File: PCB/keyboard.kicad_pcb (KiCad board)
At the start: 2 copper layers, 74 parts, among them J1 USB4510-03-1-A, J4 switch, U1 NCP1117LPST33T3G, U2 USBLC6-2SC6, U3 USBLC6-2SC6, U4 RP2040, U5 W25Q128JVS, Y1 12MHz

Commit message: Update footprint library
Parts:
- added D101: DIODE, Diode_SMD:D_SOD-123, F.Cu at (274.3, 106.7)
- added D102: DIODE, Diode_SMD:D_SOD-123, F.Cu at (262.8, 106.7)
- added D104: DIODE, Diode_SMD:D_SOD-123, F.Cu at (268.6, 110.0)
- added D105: DIODE, Diode_SMD:D_SOD-123, F.Cu at (280.1, 110.0)
- added D106: DIODE, Diode_SMD:D_SOD-123, F.Cu at (274.3, 110.0)
- added D107: DIODE, Diode_SMD:D_SOD-123, F.Cu at (280.1, 106.7)
- added D108: DIODE, Diode_SMD:D_SOD-123, F.Cu at (285.8, 106.7)
- added D109: DIODE, Diode_SMD:D_SOD-123, F.Cu at (262.8, 110.0)
- added D110: DIODE, Diode_SMD:D_SOD-123, F.Cu at (274.3, 116.7)
- added D111: DIODE, Diode_SMD:D_SOD-123, F.Cu at (268.6, 120.1)
- added D112: DIODE, Diode_SMD:D_SOD-123, F.Cu at (268.6, 113.4)
- added D113: DIODE, Diode_SMD:D_SOD-123, F.Cu at (268.6, 116.7)
- added D114: DIODE, Diode_SMD:D_SOD-123, F.Cu at (262.8, 116.7)
- added D115: DIODE, Diode_SMD:D_SOD-123, F.Cu at (268.6, 106.7)
- added D116: DIODE, Diode_SMD:D_SOD-123, F.Cu at (262.8, 113.4)
- added D117: DIODE, Diode_SMD:D_SOD-123, F.Cu at (262.8, 123.4)
- added D118: DIODE, Diode_SMD:D_SOD-123, F.Cu at (262.8, 120.1)
- added DD103: DIODE, Diode_SMD:D_SOD-123, F.Cu at (274.3, 113.4)
- added MX101: SW_Push, Footprints:CherryMX_Choc_Hotswap, F.Cu at (341.0, 47.1)
- added MX102: SW_Push, Footprints:CherryMX_Choc_Hotswap, F.Cu at (271.5, 93.4)
- added MX103: SW_Push, Footprints:CherryMX_Choc_Hotswap, F.Cu at (271.5, 70.3)
- added MX104: SW_Push, Footprints:CherryMX_Choc_Hotswap, F.Cu at (271.5, 47.1)
- added MX105: SW_Push, Footprints:CherryMX_Choc_Hotswap, F.Cu at (294.7, 93.4)
- added MX106: SW_Push, Footprints:CherryMX_Choc_Hotswap, F.Cu at (317.8, 47.1)
- added MX107: SW_Push, Footprints:CherryMX_Choc_Hotswap, F.Cu at (317.8, 70.3)
- added MX108: SW_Push, Footprints:CherryMX_Choc_Hotswap, F.Cu at (364.1, 93.4)
- added MX109: SW_Push, Footprints:CherryMX_Choc_Hotswap, F.Cu at (364.1, 47.1)
- added MX110: SW_Push, Footprints:CherryMX_Choc_Hotswap, F.Cu at (294.7, 47.1)
- added MX111: SW_Push, Footprints:CherryMX_Choc_Hotswap, F.Cu at (341.0, 70.3)
- added MX112: SW_Push, Footprints:CherryMX_Choc_Hotswap, F.Cu at (387.3, 70.3)
- added MX113: SW_Push, Footprints:CherryMX_Choc_Hotswap, F.Cu at (387.3, 93.4)
- added MX114: SW_Push, Footprints:CherryMX_Choc_Hotswap, F.Cu at (387.3, 47.1)
- added MX115: SW_Push, Footprints:CherryMX_Choc_Hotswap, F.Cu at (364.1, 70.3)
- added MX116: SW_Push, Footprints:CherryMX_Choc_Hotswap, F.Cu at (294.7, 70.3)
- added MX117: SW_Push, Footprints:CherryMX_Choc_Hotswap, F.Cu at (341.0, 93.4)
- added MX118: SW_Push, Footprints:CherryMX_Choc_Hotswap, F.Cu at (317.8, 93.4)
- added U1: TPS54202DDC, Package_TO_SOT_SMD:SOT-23-6, F.Cu at (291.3, 107.2)
- MX201: renamed from MX1; footprint Keyboard:MX -> Footprints:CherryMX_Choc_Hotswap
- MX202: renamed from MX2; footprint Keyboard:MX -> Footprints:CherryMX_Choc_Hotswap
- MX203: renamed from MX3; footprint Keyboard:MX -> Footprints:CherryMX_Choc_Hotswap
- MX204: renamed from MX4; footprint Keyboard:MX -> Footprints:CherryMX_Choc_Hotswap
- MX205: renamed from MX5; footprint Keyboard:MX -> Footprints:CherryMX_Choc_Hotswap
- MX206: renamed from MX6; footprint Keyboard:MX -> Footprints:CherryMX_Choc_Hotswap
- MX207: renamed from MX7; footprint Keyboard:MX -> Footprints:CherryMX_Choc_Hotswap
- MX208: renamed from MX8; footprint Keyboard:MX -> Footprints:CherryMX_Choc_Hotswap
- MX209: renamed from MX9; footprint Keyboard:MX -> Footprints:CherryMX_Choc_Hotswap
- MX210: renamed from MX10; footprint Keyboard:MX -> Footprints:CherryMX_Choc_Hotswap
- MX211: renamed from MX11; footprint Keyboard:MX -> Footprints:CherryMX_Choc_Hotswap
- MX212: renamed from MX12; footprint Keyboard:MX -> Footprints:CherryMX_Choc_Hotswap
- MX213: renamed from MX13; footprint Keyboard:MX -> Footprints:CherryMX_Choc_Hotswap
- MX214: renamed from MX14; footprint Keyboard:MX -> Footprints:CherryMX_Choc_Hotswap
- MX215: renamed from MX15; footprint Keyboard:MX -> Footprints:CherryMX_Choc_Hotswap
- MX216: renamed from MX16; footprint Keyboard:MX -> Footprints:CherryMX_Choc_Hotswap
- MX217: renamed from MX17; footprint Keyboard:MX -> Footprints:CherryMX_Choc_Hotswap
- MX218: renamed from MX18; footprint Keyboard:MX -> Footprints:CherryMX_Choc_Hotswap
- U5: value W25Q128JVS -> W25Q128JVSIQ
- renumbered D3 to D201, D2 to D202, D1 to D203, D6 to D204, D5 to D205, D4 to D206, D9 to D207, D8 to D208, D7 to D209, D12 to D210, D11 to D211, D10 to D212, D15 to D213, D14 to D214, D13 to D215, D18 to D216, D17 to D217, D16 to D218, J1 to J101, R8 to R108, R9 to R109
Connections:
- C16 pad 1: Net-(C16-Pad1) -> /XIN
- D201 pad 1: ROW1 -> L-ROW-1
- D202 pad 1: ROW2 -> L-ROW-2
- D203 pad 1: ROW3 -> L-ROW-3
- D204 pad 1: ROW1 -> L-ROW-1
- D205 pad 1: ROW2 -> L-ROW-2
- D206 pad 1: ROW3 -> L-ROW-3
- D207 pad 1: ROW1 -> L-ROW-1
- D208 pad 1: ROW2 -> L-ROW-2
- D209 pad 1: ROW3 -> L-ROW-3
- D210 pad 1: ROW1 -> L-ROW-1
- D211 pad 1: ROW2 -> L-ROW-2
- D212 pad 1: ROW3 -> L-ROW-3
- D213 pad 1: ROW1 -> L-ROW-1
- D214 pad 1: ROW2 -> L-ROW-2
- D215 pad 1: ROW3 -> L-ROW-3
- D216 pad 1: ROW1 -> L-ROW-1
- D217 pad 1: ROW2 -> L-ROW-2
- D218 pad 1: ROW3 -> L-ROW-3
- MX201 pad 1: COL1 -> L-COL-1
- MX202 pad 1: COL1 -> L-COL-1
- MX203 pad 1: COL1 -> L-COL-1
- MX204 pad 1: COL2 -> L-COL-2
- MX205 pad 1: COL2 -> L-COL-2
- MX206 pad 1: COL2 -> L-COL-2
- MX207 pad 1: COL3 -> L-COL-3
- MX208 pad 1: COL3 -> L-COL-3
- MX209 pad 1: COL3 -> L-COL-3
- MX210 pad 1: COL4 -> L-COL-4
- MX211 pad 1: COL4 -> L-COL-4
- MX212 pad 1: COL4 -> L-COL-4
- MX213 pad 1: COL5 -> L-COL-5
- MX214 pad 1: COL5 -> L-COL-5
- MX215 pad 1: COL5 -> L-COL-5
- MX216 pad 1: COL6 -> L-COL-6
- MX217 pad 1: COL6 -> L-COL-6
- MX218 pad 1: COL6 -> L-COL-6
- Y1 pad 1: Net-(C16-Pad1) -> /XIN
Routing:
- net ROW2: track 95.0 -> 0.00 mm, vias 5 -> 0
- net L-ROW-2: track 0.00 -> 95.0 mm, vias 0 -> 5
- net L-ROW-3: track 0.00 -> 94.6 mm, vias 0 -> 3
- net ROW1: track 91.8 -> 0.00 mm, vias 5 -> 0
- net L-ROW-1: track 0.00 -> 91.8 mm, vias 0 -> 5
- net ROW3: track 90.2 -> 0.00 mm, vias 3 -> 0
- net L-COL-5: track 0.00 -> 47.1 mm
- net L-COL-3: track 0.00 -> 42.6 mm
- net L-COL-2: track 0.00 -> 38.1 mm
- net COL2: track 38.1 -> 0.00 mm
- net L-COL-1: track 0.00 -> 38.1 mm
- net COL1: track 38.1 -> 0.00 mm
- net L-COL-4: track 0.00 -> 38.1 mm
- net COL5: track 38.1 -> 0.00 mm
- net COL4: track 38.1 -> 0.00 mm
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
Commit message: wip full sch
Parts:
- D101, D102, D104, D105, D106, D107, D108, D109, D110, D111, D112, D113, D114, D115, D116, D117, D118, DD103: moved to B.Cu
- moved C13 124.1 mm to (168.6, 61.0), turned to 90 degrees
- moved C14 120.4 mm to (166.3, 61.0), turned to 90 degrees
- moved U1 106.2 mm to (193.2, 66.5), turned to 90 degrees
- moved D113 106.0 mm to (353.9, 53.8), turned to 90 degrees
- moved J4 102.6 mm to (193.2, 53.0)
- moved D114 101.1 mm to (353.9, 72.8), turned to 90 degrees
- moved C11 88.0 mm to (155.5, 124.3)
- moved C12 88.0 mm to (152.6, 124.3)
- moved C16 88.0 mm to (149.8, 124.3)
- moved C7 88.0 mm to (158.4, 124.3)
- moved R109 88.0 mm to (169.9, 124.3)
- moved R13 88.0 mm to (178.6, 124.3)
- moved R5 88.0 mm to (172.8, 124.3)
- moved R7 88.0 mm to (181.5, 124.3)
- moved C6 88.0 mm to (161.3, 124.3)
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
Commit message: latest changes
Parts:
- removed C1, C2: 10u, Capacitor_SMD:C_0603_1608Metric
- removed C10, C11, C12, C15, C4, C5, C6, C7, C8, C9: 100n, Capacitor_SMD:C_0402_1005Metric
- removed C13, C14: 1u, Capacitor_SMD:C_0402_1005Metric
- removed C16, C17: 20p, Capacitor_SMD:C_0402_1005Metric
- removed C3: 10u, Capacitor_SMD:C_0805_2012Metric
- removed D19: C2480, Diode_SMD:D_SMA
- removed DD103: DIODE, Diode_SMD:D_SOD-123
- removed F2: 1000mA, Fuse:Fuse_1206_3216Metric
- removed J4: switch, Connector_PinHeader_2.54mm:PinHeader_1x02_P2.54mm_Vertical
- removed R1, R2: 5.1k, Resistor_SMD:R_0603_1608Metric
- removed R12, R13: 2.2K, Resistor_SMD:R_0402_1005Metric
- removed R3, R4: 27, Resistor_SMD:R_0402_1005Metric
- removed R5: 10k, Resistor_SMD:R_0402_1005Metric
- removed R6, R7: 1k, Resistor_SMD:R_0402_1005Metric
- removed U1: TPS54202DDC, Package_TO_SOT_SMD:SOT-23-6
- removed U1: NCP1117LPST33T3G, NCP1117LPST33T3G:NCP1117LPST33T3G
- removed U2, U3: USBLC6-2SC6, Package_TO_SOT_SMD:SOT-23-6
- removed U4: RP2040, RP2040:SC090813
- removed U5: W25Q128JVSIQ, Package_SO:SOIC-8_5.23x5.23mm_P1.27mm
- removed Y1: 12MHz, Oscillator:Oscillator_SMD_Abracon_ASE-4Pin_3.2x2.5mm
- added C101: 20p, Capacitor_SMD:C_0402_1005Metric, B.Cu at (152.5, 170.2)
- added C102: 100n, Capacitor_SMD:C_0402_1005Metric, B.Cu at (160.1, 149.2)
- added C103: 1u, Capacitor_SMD:C_0402_1005Metric, B.Cu at (146.6, 154.3)
- added C104: 20p, Capacitor_SMD:C_0402_1005Metric, B.Cu at (150.9, 167.6)
- added C105: 100n, Capacitor_SMD:C_0402_1005Metric, B.Cu at (146.6, 156.3)
- added C106: 100n, Capacitor_SMD:C_0402_1005Metric, B.Cu at (143.1, 152.5)
- added C107: 100n, Capacitor_SMD:C_0402_1005Metric, B.Cu at (146.6, 155.3)
- added C108: 100n, Capacitor_SMD:C_0402_1005Metric, B.Cu at (140.4, 155.8)
- added C109: 100n, Capacitor_SMD:C_0402_1005Metric, B.Cu at (140.4, 156.9)
- added C110: 100n, Capacitor_SMD:C_0402_1005Metric, B.Cu at (140.3, 158.4)
- added C111: 100n, Capacitor_SMD:C_0402_1005Metric, B.Cu at (140.3, 160.0)
- added C112: 100n, Capacitor_SMD:C_0402_1005Metric, B.Cu at (153.0, 152.7)
- added C113: 100n, Capacitor_SMD:C_0402_1005Metric, B.Cu at (147.8, 163.8)
- added C114: 1u, Capacitor_SMD:C_0402_1005Metric, B.Cu at (150.0, 152.7)
- added C115: 10u, Capacitor_SMD:C_0805_2012Metric, F.Cu at (138.7, 128.3)
- added C116: 22uF, Capacitor_SMD:C_0805_2012Metric, F.Cu at (142.4, 125.6)
- added C201: 20p, Capacitor_SMD:C_0402_1005Metric, F.Cu at (195.8, 27.4)
- added C202: 100n, Capacitor_SMD:C_0402_1005Metric, F.Cu at (184.3, 40.2)
- added C203: 1u, Capacitor_SMD:C_0402_1005Metric, F.Cu at (189.2, 34.6)
- added C204: 20p, Capacitor_SMD:C_0402_1005Metric, F.Cu at (185.5, 38.2)
- added C205: 100n, Capacitor_SMD:C_0402_1005Metric, F.Cu at (198.7, 21.0)
- added C206: 100n, Capacitor_SMD:C_0402_1005Metric, F.Cu at (192.0, 31.9)
- added C207: 100n, Capacitor_SMD:C_0402_1005Metric, F.Cu at (199.3, 24.9)
- added C208: 100n, Capacitor_SMD:C_0402_1005Metric, F.Cu at (189.2, 32.6)
- added C209: 100n, Capacitor_SMD:C_0402_1005Metric, F.Cu at (201.6, 21.0)
- added C210: 100n, Capacitor_SMD:C_0402_1005Metric, F.Cu at (181.5, 40.2)
- added C211: 100n, Capacitor_SMD:C_0402_1005Metric, F.Cu at (198.7, 23.0)
- added C212: 100n, Capacitor_SMD:C_0402_1005Metric, F.Cu at (196.5, 24.9)
- added C213: 100n, Capacitor_SMD:C_0402_1005Metric, F.Cu at (185.5, 36.2)
- added C214: 1u, Capacitor_SMD:C_0402_1005Metric, F.Cu at (192.9, 29.9)
- added C215: 10u, Capacitor_SMD:C_0805_2012Metric, F.Cu at (231.0, 29.3)
- added C216: 22uF, Capacitor_SMD:C_0805_2012Metric, F.Cu at (226.3, 33.9)
- added D103: DIODE, Diode_SMD:D_SOD-123, B.Cu at (40.4, 157.5)
- added D119: LED, LED_SMD:LED_0603_1608Metric, B.Cu at (140.9, 116.4)
- added D120: LED, LED_SMD:LED_0603_1608Metric, B.Cu at (150.4, 144.1)
- added D219: LED, LED_SMD:LED_0603_1608Metric, F.Cu at (172.2, 39.8)
- added D220: LED, LED_SMD:LED_0603_1608Metric, F.Cu at (168.2, 39.8)
- added J102: switch, Connector_PinHeader_2.54mm:PinHeader_1x02_P2.54mm_Vertical, F.Cu at (167.3, 141.0)
- added J103: USB4510-03-1-A, USB4510-03-1-A:USB4510-03-1-A, B.Cu at (155.9, 107.7)
- added J105: AudioJack4, Footprints:TRRS-PJ-320A, F.Cu at (204.2, 156.7)
- added J201: switch, Connector_PinHeader_2.54mm:PinHeader_1x02_P2.54mm_Vertical, F.Cu at (185.8, 22.3)
- added J202: switch, Connector_PinHeader_2.54mm:PinHeader_1x02_P2.54mm_Vertical, F.Cu at (178.8, 34.1)
- added J203: USB4510-03-1-A, USB4510-03-1-A:USB4510-03-1-A, F.Cu at (175.0, 26.5)
- added J205: AudioJack4, Footprints:TRRS-PJ-320A, F.Cu at (213.8, 37.6)
- added L101: 2.2μH, Inductor_SMD:L_Taiyo-Yuden_NR-30xx, F.Cu at (147.5, 126.9)
- added L201: 2.2μH, Inductor_SMD:L_Taiyo-Yuden_NR-30xx, F.Cu at (226.4, 30.1)
- added R101: 2.2K, Resistor_SMD:R_0402_1005Metric, B.Cu at (137.7, 117.2)
- added R102: 2.2K, Resistor_SMD:R_0402_1005Metric, B.Cu at (132.1, 146.2)
- added R103: 1k, Resistor_SMD:R_0402_1005Metric, B.Cu at (127.0, 141.8)
- added R104: 1k, Resistor_SMD:R_0402_1005Metric, B.Cu at (152.7, 164.7)
- added R105: 27, Resistor_SMD:R_0402_1005Metric, B.Cu at (152.0, 152.7)
- added R106: 27, Resistor_SMD:R_0402_1005Metric, B.Cu at (151.0, 152.7)
- added R107: 5.1k, Resistor_SMD:R_0603_1608Metric, B.Cu at (152.0, 116.1)
- added R110: 100k, Resistor_SMD:R_0603_1608Metric, F.Cu at (145.5, 130.9)
- added R111: 5.1k, Resistor_SMD:R_0603_1608Metric, B.Cu at (159.8, 116.2)
- added R201: 2.2K, Resistor_SMD:R_0402_1005Metric, F.Cu at (178.6, 39.9)
- added R202: 2.2K, Resistor_SMD:R_0402_1005Metric, F.Cu at (182.6, 36.2)
- added R203: 1k, Resistor_SMD:R_0402_1005Metric, F.Cu at (192.9, 28.0)
- added R204: 1k, Resistor_SMD:R_0402_1005Metric, F.Cu at (182.6, 38.2)
- added R205: 27, Resistor_SMD:R_0402_1005Metric, F.Cu at (193.6, 25.4)
- added R206: 27, Resistor_SMD:R_0402_1005Metric, F.Cu at (190.0, 29.9)
- added R207: 5.1k, Resistor_SMD:R_0603_1608Metric, F.Cu at (190.1, 25.7)
- added R208: 4.7K, Resistor_SMD:R_0402_1005Metric, F.Cu at (175.7, 39.9)
- added R209: 4.7K, Resistor_SMD:R_0402_1005Metric, F.Cu at (190.0, 28.0)
- added R210: 100k, Resistor_SMD:R_0603_1608Metric, F.Cu at (230.5, 33.7)
- added R211: 5.1k, Resistor_SMD:R_0603_1608Metric, F.Cu at (195.3, 21.3)
- added U101: W25Q128JVSIQ, Package_SO:SOIC-8_5.23x5.23mm_P1.27mm, B.Cu at (162.6, 157.4)
- added U102: RP2040, RP2040:SC090813, B.Cu at (152.7, 159.1)
- added U103: TPS62172DSG, Package_SON:WSON-8-1EP_2x2mm_P0.5mm_EP0.9x1.6mm_ThermalVias, F.Cu at (142.4, 129.2)
- added U104: USBLC6-2SC6, Package_TO_SOT_SMD:SOT-23-6, B.Cu at (155.8, 117.0)
- added U105: USBLC6-2SC6, Package_TO_SOT_SMD:SOT-23-6, B.Cu at (135.4, 157.5)
- added U201: W25Q128JVSIQ, Package_SO:SOIC-8_5.23x5.23mm_P1.27mm, F.Cu at (171.3, 35.1)
- added U202: RP2040, RP2040:SC090813, F.Cu at (203.3, 41.0)
- added U203: TPS62172DSG, Package_SON:WSON-8-1EP_2x2mm_P0.5mm_EP0.9x1.6mm_ThermalVias, F.Cu at (185.6, 33.4)
- added U204: USBLC6-2SC6, Package_TO_SOT_SMD:SOT-23-6, F.Cu at (190.7, 22.2)
- added U205: USBLC6-2SC6, Package_TO_SOT_SMD:SOT-23-6, F.Cu at (224.3, 22.2)
- added Y101: 12MHz, Oscillator:Oscillator_SMD_Abracon_ASE-4Pin_3.2x2.5mm, B.Cu at (153.7, 167.6)
- added Y201: 12MHz, Oscillator:Oscillator_SMD_Abracon_ASE-4Pin_3.2x2.5mm, F.Cu at (186.0, 29.4)
- D201, D202, D203, D204, D205, D206, D207, D208, D209, D210, D211, D212, D213, D214, D215, D216, D217, D218: moved to F.Cu
- J101: value USB4510-03-1-A -> switch; footprint USB4510-03-1-A:USB4510-03-1-A -> Connector_PinHeader_2.54mm:PinHeader_1x02_P2.54mm_Vertical; moved to F.Cu
- moved D107 246.4 mm to (78.4, 119.5)
- moved D104 246.4 mm to (59.4, 119.5)
- moved D105 246.4 mm to (59.4, 138.5)
- moved D106 246.4 mm to (59.4, 157.5)
- moved D113 246.4 mm to (116.4, 119.5)
- moved D114 246.4 mm to (116.4, 138.5)
- moved D115 246.4 mm to (116.4, 157.5)
- moved D108 246.4 mm to (78.4, 138.5)
- moved D109 246.4 mm to (78.4, 157.5)
- moved D101 246.4 mm to (40.4, 119.5)
- moved D102 246.4 mm to (40.4, 138.5)
- moved D110 246.4 mm to (97.4, 119.5)
- moved D111 246.4 mm to (97.4, 138.5)
- moved D112 246.4 mm to (97.4, 157.5)
- moved MX104 245.4 mm to (52.3, 112.4)
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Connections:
- net L-COL-1 renamed /Right MCU/COL-1
- net L-COL-2 renamed /Right MCU/COL-2
- net R-COL-1 renamed /Left MCU/COL-1
- net R-COL-2 renamed /Left MCU/COL-2
- D101 pad 1: R-ROW-1 -> /Left MCU/ROW-1
- D102 pad 1: R-ROW-2 -> /Left MCU/ROW-2
- D104 pad 1: R-ROW-1 -> /Left MCU/ROW-1
- D105 pad 1: R-ROW-2 -> /Left MCU/ROW-2
- D106 pad 1: R-ROW-3 -> /Left MCU/ROW-3
- D107 pad 1: R-ROW-1 -> /Left MCU/ROW-1
- D108 pad 1: R-ROW-2 -> /Left MCU/ROW-2
- D109 pad 1: R-ROW-3 -> /Left MCU/ROW-3
- D110 pad 1: R-ROW-1 -> /Left MCU/ROW-1
- D111 pad 1: R-ROW-2 -> /Left MCU/ROW-2
- D112 pad 1: R-ROW-3 -> /Left MCU/ROW-3
- D113 pad 1: R-ROW-1 -> /Left MCU/ROW-1
- D114 pad 1: R-ROW-2 -> /Left MCU/ROW-2
- D115 pad 1: R-ROW-3 -> /Left MCU/ROW-3
- D116 pad 1: R-ROW-1 -> /Left Matix/ROW-4
- D117 pad 1: R-ROW-2 -> /Left Matix/ROW-4
- D118 pad 1: R-ROW-3 -> /Left Matix/ROW-4
- D201 pad 1: L-ROW-1 -> /Right MCU/ROW-1
- D202 pad 1: L-ROW-2 -> /Right MCU/ROW-2
- D203 pad 1: L-ROW-3 -> /Right MCU/ROW-3
- D204 pad 1: L-ROW-1 -> /Right MCU/ROW-1
- D205 pad 1: L-ROW-2 -> /Right MCU/ROW-2
- D206 pad 1: L-ROW-3 -> /Right MCU/ROW-3
- D207 pad 1: L-ROW-1 -> /Right MCU/ROW-1
- D208 pad 1: L-ROW-2 -> /Right MCU/ROW-2
- D209 pad 1: L-ROW-3 -> /Right MCU/ROW-3
- D210 pad 1: L-ROW-1 -> /Right MCU/ROW-1
- D211 pad 1: L-ROW-2 -> /Right MCU/ROW-2
- D212 pad 1: L-ROW-3 -> /Right MCU/ROW-3
- D213 pad 1: L-ROW-1 -> /Right MCU/ROW-1
- D214 pad 1: L-ROW-2 -> /Right MCU/ROW-2
- D215 pad 1: L-ROW-3 -> /Right MCU/ROW-3
- D216 pad 1: L-ROW-1 -> /Right Matrix/ROW-4
- D217 pad 1: L-ROW-2 -> /Right Matrix/ROW-4
- D218 pad 1: L-ROW-3 -> /Right Matrix/ROW-4
- MX107 pad 1: R-COL-3 -> /Left MCU/COL-3
- MX108 pad 1: R-COL-3 -> /Left MCU/COL-3
- MX109 pad 1: R-COL-3 -> /Left MCU/COL-3
- MX110 pad 1: R-COL-4 -> /Left MCU/COL-4
- MX111 pad 1: R-COL-4 -> /Left MCU/COL-4
- MX112 pad 1: R-COL-4 -> /Left MCU/COL-4
- MX113 pad 1: R-COL-5 -> /Left MCU/COL-5
- MX114 pad 1: R-COL-5 -> /Left MCU/COL-5
- MX115 pad 1: R-COL-5 -> /Left MCU/COL-5
- MX116 pad 1: R-COL-6 -> /Left MCU/COL-3
- MX117 pad 1: R-COL-6 -> /Left MCU/COL-4
- MX118 pad 1: R-COL-6 -> /Left MCU/COL-5
- MX207 pad 1: L-COL-3 -> /Right MCU/COL-3
- MX208 pad 1: L-COL-3 -> /Right MCU/COL-3
- MX209 pad 1: L-COL-3 -> /Right MCU/COL-3
- MX210 pad 1: L-COL-4 -> /Right MCU/COL-4
- MX211 pad 1: L-COL-4 -> /Right MCU/COL-4
- MX212 pad 1: L-COL-4 -> /Right MCU/COL-4
- MX213 pad 1: L-COL-5 -> /Right MCU/COL-5
- MX214 pad 1: L-COL-5 -> /Right MCU/COL-5
- MX215 pad 1: L-COL-5 -> /Right MCU/COL-5
- MX216 pad 1: L-COL-6 -> /Right MCU/COL-3
- MX217 pad 1: L-COL-6 -> /Right MCU/COL-4
- MX218 pad 1: L-COL-6 -> /Right MCU/COL-5
- R108 pad 1: SDA_DISPLAY -> /Left MCU/SDA
- R109 pad 1: SCL_DISPLAY -> /Left MCU/SCL
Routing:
- net L-ROW-2: track 95.0 -> 0.00 mm, vias 5 -> 0
- net L-ROW-3: track 94.6 -> 0.00 mm, vias 3 -> 0
- net L-ROW-1: track 91.8 -> 0.00 mm, vias 5 -> 0
- net L-COL-5: track 47.1 -> 0.00 mm
- net L-COL-3: track 42.6 -> 0.00 mm
- net /Right MCU/COL-2: track 38.1 -> 0.00 mm
- net /Right MCU/COL-1: track 38.1 -> 0.00 mm
- net L-COL-4: track 38.1 -> 0.00 mm
- net /Left MCU/QSPI_SCLK: track 0.00 -> 28.7 mm
- net /Left MCU/QSPI_SD0: track 0.00 -> 23.7 mm
- net +3V3: track 0.00 -> 13.8 mm
- net /Left MCU/QSPI_SD2: track 0.00 -> 13.4 mm
- net Net-(D207-Pad2): track 11.2 -> 0.00 mm
- net /Left MCU/QSPI_SD1: track 0.00 -> 10.7 mm
- net /Left MCU/XIN: track 0.00 -> 10.4 mm
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
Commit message: Power and USB
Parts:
- C115, C116, L101, R110, U103: moved to B.Cu
- moved C116 7.21 mm to (145.5, 132.1)
- moved R110 4.90 mm to (147.1, 126.2), turned to 180 degrees
- moved L101 3.85 mm to (149.4, 130.3), turned to -90 degrees
- moved C115 3.75 mm to (142.2, 129.5), turned to -90 degrees
- moved U103 2.80 mm to (145.2, 129.2)
- moved R111 0.38 mm to (160.1, 116.2), turned to 180 degrees
- turned R107 to 180 degrees
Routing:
- net +3V3: track 13.8 -> 23.1 mm, vias 0 -> 2
- net /Left MCU/USB_CONN_D-: track 4.43 -> 12.0 mm, vias 0 -> 2
- net /Left MCU/USB_CONN_D+: track 4.47 -> 11.6 mm, vias 0 -> 2
- net Net-(J103-PadB5): track 0.00 -> 5.24 mm
- net Net-(J103-PadA5): track 0.00 -> 5.20 mm
- net Net-(R110-Pad2): track 0.00 -> 5.18 mm, vias 0 -> 2
- net VBUS: track 7.35 -> 3.81 mm
- net GND: track 6.13 -> 9.59 mm, vias 1 -> 2
- added copper zone on B.Cu, net +3V3
- added copper zone on B.Cu, net GND
- added copper zone on B.Cu, net Net-(L101-Pad1)
- added copper zone on B.Cu, net VBUS

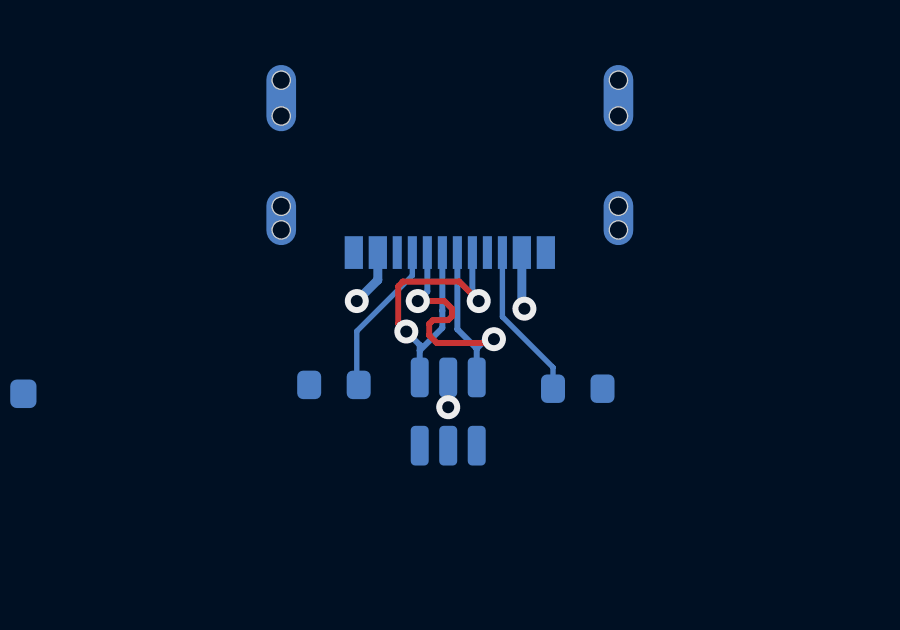
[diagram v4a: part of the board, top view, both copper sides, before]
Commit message: Swap usb pair
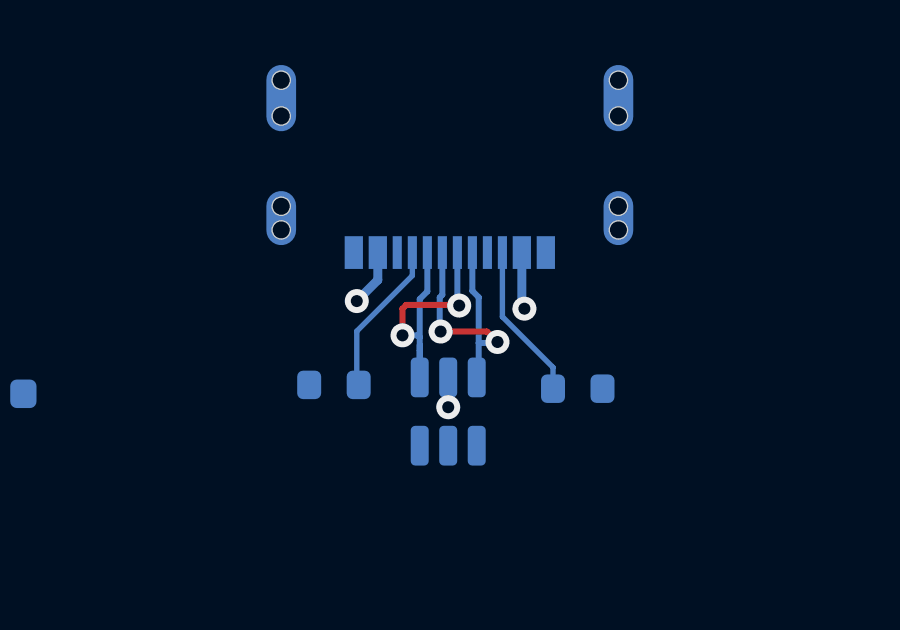
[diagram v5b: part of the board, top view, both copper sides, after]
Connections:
- U104 pad 1: /Left MCU/USB_CONN_D+ -> /Left MCU/USB_CONN_D-
- U104 pad 3: /Left MCU/USB_CONN_D- -> /Left MCU/USB_CONN_D+
- U104 pad 4: /Left MCU/USB_D- -> /Left MCU/USB_D+
- U104 pad 6: /Left MCU/USB_D+ -> /Left MCU/USB_D-
- U204 pad 1: /Right MCU/USB_CONN_D+ -> /Right MCU/USB_CONN_D-
- U204 pad 3: /Right MCU/USB_CONN_D- -> /Right MCU/USB_CONN_D+
- U204 pad 4: /Right MCU/USB_D- -> /Right MCU/USB_D+
- U204 pad 6: /Right MCU/USB_D+ -> /Right MCU/USB_D-
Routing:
- net /Left MCU/USB_CONN_D+: track 11.6 -> 9.64 mm
- net /Left MCU/USB_CONN_D-: track 12.0 -> 10.6 mm

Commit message: More work on MCU
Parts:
- moved U105 31.6 mm to (166.9, 158.8)
- moved J105 23.3 mm to (181.6, 151.4)
- moved C111 17.9 mm to (158.2, 160.1), turned to 0 degrees
- moved D120 13.8 mm to (140.7, 153.8)
- moved C110 13.5 mm to (151.8, 165.5), turned to -90 degrees
- moved C107 11.7 mm to (158.2, 156.5), turned to 0 degrees
- moved C106 10.2 mm to (153.4, 152.1)
- moved C109 6.43 mm to (146.6, 155.2)
- moved C108 6.20 mm to (146.6, 156.4)
- moved U101 5.92 mm to (160.8, 151.7), turned to 180 degrees
- moved R101 5.22 mm to (142.8, 116.0)
- moved C101 4.68 mm to (156.1, 167.1), turned to 0 degrees
- moved D119 3.99 mm to (143.1, 119.7)
- moved C105 3.97 mm to (147.7, 160.1)
- moved R109 3.67 mm to (160.5, 167.6)
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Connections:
- U102 pad 2: /TRRS Connection/L_TX -> /Left MCU/TX
- U102 pad 3: /TRRS Connection/L_RX -> /Left MCU/RX
- U105 pad 1: /TRRS Connection/L_RX -> /TRRS Connection/L_RX_CONN
- U105 pad 3: /TRRS Connection/L_TX -> /TRRS Connection/L_TX_CONN
- U105 pad 4: /TRRS Connection/L_TX -> /Left MCU/TX
- U105 pad 6: /TRRS Connection/L_RX -> /Left MCU/RX
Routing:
- net /Left MCU/USB_D-: track 0.00 -> 34.7 mm
- net /Left MCU/USB_D+: track 0.00 -> 34.7 mm
- net VBUS: track 3.81 -> 37.7 mm, vias 2 -> 4
- net GND: track 9.59 -> 37.7 mm, vias 2 -> 27
- net /Left MCU/QSPI_SCLK: track 28.7 -> 5.32 mm
- net /Left MCU/QSPI_SD0: track 23.7 -> 4.28 mm
- net +1V1: track 5.17 -> 17.6 mm, vias 0 -> 4
- net +3V3: track 23.1 -> 32.9 mm
- net /Left MCU/QSPI_SS: track 9.39 -> 16.8 mm
- net /Left MCU/QSPI_SD3: track 0.00 -> 6.89 mm
- net /Left MCU/QSPI_SD1: track 10.7 -> 15.9 mm
- net /Left MCU/SCL: track 0.00 -> 3.79 mm
- net /Left MCU/SDA: track 0.00 -> 3.19 mm
- net /Left MCU/QSPI_SD2: track 13.4 -> 11.6 mm
- net /Left MCU/XOUT: track 1.80 -> 3.59 mm
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- added copper zone on B.Cu, net +1V1
- added copper zone on F.Cu, net GND

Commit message: add stagger, crude outline
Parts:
- moved C201 673.6 mm to (868.9, 52.7)
- moved C203 673.6 mm to (862.3, 59.9)
- moved C206 673.6 mm to (865.1, 57.2)
- moved C208 673.6 mm to (862.3, 57.9)
- moved C214 673.6 mm to (866.0, 55.2)
- moved C215 673.6 mm to (904.1, 54.6)
- moved C216 673.6 mm to (899.4, 59.2)
- moved D201 673.6 mm to (699.1, 117.5)
- moved D202 673.6 mm to (704.9, 120.8)
- moved D203 673.6 mm to (716.4, 110.8)
- moved D204 673.6 mm to (704.9, 107.4)
- moved D205 673.6 mm to (704.9, 114.1)
- moved D206 673.6 mm to (704.9, 117.5)
- moved D207 673.6 mm to (699.1, 110.8)
- moved D208 673.6 mm to (722.1, 107.4)
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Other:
- board outline added: 125.1 x 102.1 mm

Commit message: less crude outline
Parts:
- added J104: CONN_DISPLAY, Footprints:OLED_128_64, F.Cu at (198.2, 55.7)
- added J204: CONN_DISPLAY, Footprints:OLED_128_64, F.Cu at (644.7, 56.5)
- moved C101 116.9 mm to (140.3, 92.2)
- moved C104 116.9 mm to (138.4, 92.2)
- moved C105 116.9 mm to (132.0, 85.2)
- moved C106 116.9 mm to (137.6, 77.2)
- moved C110 116.9 mm to (136.1, 90.5)
- moved C111 116.9 mm to (142.5, 85.1)
- moved C112 116.9 mm to (138.7, 77.2)
- moved C113 116.9 mm to (135.0, 90.5)
- moved C115 116.9 mm to (126.5, 54.6)
- moved C116 116.9 mm to (129.8, 57.1)
- moved D119 116.9 mm to (127.4, 44.7)
- moved J102 116.9 mm to (151.5, 66.0)
- moved J105 116.9 mm to (165.9, 76.4)
- moved L101 116.9 mm to (133.6, 55.3)
- moved R106 116.9 mm to (135.3, 77.7)
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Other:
- board size 125.1 x 102.1 mm -> 125.5 x 102.1 mm
